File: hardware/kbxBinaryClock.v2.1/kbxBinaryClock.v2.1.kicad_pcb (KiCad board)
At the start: 2 copper layers, 127 x 114.3 mm, 137 parts, among them J1 Jack-DC, J2 Conn_01x06, J3 Conn_02x03_Odd_Even, P1 STM32_SWD_USART, Q1 2N7002, Q10 Q_NPN_BCE, Q11 Q_NPN_BCE, Q2 2N7002, Q3 2N7002, Q4 2N7002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

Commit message: Updated Silkscreen for volume mode and added clearer pin 1 markings for ICs
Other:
- board text added: "."
- board text added: "RESET SUPERVISOR"
- board text added: "RGB Binary Clock version 2.1.3 Designed by Keith Burzinski (@kbx81) in Chicago, Illinois Source & other details: https://github.com/kbx81/RGBBinaryClock Layout inspired by EKI, Inc. kit 798"
- board text removed: "RGB Binary Clock version 2.1.2 Designed by Keith Burzinski (@kbx81) in Chicago, Illinois Source & other details: https://github.com/kbx81/RGBBinaryClock Layout inspired by EKI, Inc. kit 798"
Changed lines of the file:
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@@
     (area 92.151429 32.944999 222.808572 147.514525)
     (thickness 1.6)
-    (drawings 33)
+    (drawings 41)
     (tracks 2921)
     (zones 0)
@@
       (net 158 "Net-(SB2-Pad2)"))
   )
+  (gr_text "RESET\nSUPERVISOR" (at 175.641 121.158) (layer B.SilkS)
+    (effects (font (size 0.75 0.75) (thickness 0.15)) (justify mirror))
+  )
+  (gr_text . (at 144.145 114.3) (layer F.SilkS)
+    (effects (font (size 2 2) (thickness 0.5)))
+  )
+  (gr_text . (at 160.528 117.475) (layer F.SilkS)
+    (effects (font (size 2 2) (thickness 0.5)))
+  )
+  (gr_text . (at 172.72 114.935) (layer F.SilkS)
+    (effects (font (size 2 2) (thickness 0.5)))
+  )
+  (gr_text . (at 200.787 89.789) (layer F.SilkS)
+    (effects (font (size 2 2) (thickness 0.5)))
+  )
+  (gr_text . (at 177.546 103.632) (layer F.SilkS)
+    (effects (font (size 2 2) (thickness 0.5)))
+  )
+  (gr_text . (at 147.066 103.632) (layer F.SilkS)
+    (effects (font (size 2 2) (thickness 0.5)))
+  )
+  (gr_text . (at 116.586 103.632) (layer F.SilkS)
+    (effects (font (size 2 2) (thickness 0.5)))
+  )
   (gr_text "9 to 12 Volts DC\n2 Amps\nPositive (+) Tip" (at 217.17 135.382) (layer B.SilkS)
     (effects (font (size 0.75 0.75) (thickness 0.15)) (justify left mirror))
@@
     (effects (font (size 1 1) (thickness 0.15)) (justify mirror))
   )
-  (gr_text "Touch Key Usage\n===========\n+ In Any Mode:\n A: Apply/Save\n E: Exit to Menu\n+ In \"Set Time\" Modes:\n C: Select Hour/Minute/Second\n D/U: Decrease/Increase Selected Value\n+ In \"Set Value\" Modes:\n B: Set Minimum for Value\n C: Set Maximum for Value\n D/U: Decrease/Increase Value\n+ In \"Set Color\" Modes:\n B: Select Value to Increase/Decrease by\n C: Select Color Element\n D/U: Decrease/Increase Selected Color Element\n+ In \"Set Bits\" Modes:\n B: Clear Selected Bit\n C: Set Selected Bit\n D/U: Select Previous/Next Bit" (at 187.325 131.572) (layer B.SilkS)
+  (gr_text "Touch Key Usage\n===========\n+ In Any Mode:\n A: Apply/Save\n E: Exit to Menu\n+ In \"Set Time\" Modes:\n C: Select Hour/Minute/Second\n D/U: Decrease/Increase Selected Value\n+ In \"Set Value\" Modes:\n B: Set Minimum for Value\n C: Set Maximum for Value\n D/U: Decrease/Increase Value\n+ In \"Set Color\" Modes:\n B: Select Value to Increase/Decrease by\n C: Select Color Element\n D/U: Decrease/Increase Selected Color Element\n+ In \"Set Bits\" Modes:\n B: Clear Selected Bit\n C: Set Selected Bit\n D/U: Select Previous/Next Bit" (at 170.307 130.556) (layer B.SilkS)
     (effects (font (size 0.75 0.75) (thickness 0.15)) (justify left mirror))
   )
-  (gr_text "Modes:\n====\n1: Fixed Display\n2: Toggle Display\n3: Timer/Counter\n5: Set Time\n6: Set Date\n10: Set System Options/Config Bits\n11: Set Slot Beep Enable Bits\n12: Set Slot Blink Enable Bits\n13: Set Slot Color Change Enable Bits\n20: Set Duration of Time Display Value (in Toggle Mode 2)\n21: Set Duration of Date Display Value (in Toggle Mode 2)\n22: Set Duration of Temperature Display Value (in Toggle Mode 2)\n23: Set Duration of Fade as Bits Change Value\n24: Set DST Begin Month Value\n25: Set DST Begin Day of Week Ordinal Value\n26: Set DST End Month Value\n27: Set DST End Day of Week Ordinal Value\n28: Set DST Switch Day of Week Value\n29: Set DST Switch Hour Value\n30: Set Minimum Display Intensity Value\n31: Set Flicker Reduction Threshold Value\n32: Set Current Drive Level Value\n33: Set Temperature Calibration Value\n34: Set DMX-512 Address Value\n40 - 47: Set Slot 1 through 8 Time\n50 - 57: Set Slot 1 through 8 Colors\n58: Set Date Colors\n59: Set Temperature Colors\n60: Set Timer/Counter Colors" (at 207.518 101.981) (layer B.SilkS)
+  (gr_text "Modes:\n====\n1: Fixed Display\n2: Toggle Display\n3: Timer/Counter\n5: Set Time\n6: Set Date\n10: Set System Options/Config Bits\n11: Set Slot Beep Enable Bits\n12: Set Slot Blink Enable Bits\n13: Set Slot Color Change Enable Bits\n20: Set Duration of Time Display Value (in Toggle Mode 2)\n21: Set Duration of Date Display Value (in Toggle Mode 2)\n22: Set Duration of Temperature Display Value (in Toggle Mode 2)\n23: Set Duration of Fade as Bits Change Value\n24: Set DST Begin Month Value\n25: Set DST Begin Day of Week Ordinal Value\n26: Set DST End Month Value\n27: Set DST End Day of Week Ordinal Value\n28: Set DST Switch Day of Week Value\n29: Set DST Switch Hour Value\n30: Set Minimum Display Intensity Value\n31: Set Flicker Reduction Threshold Value\n32: Set Current Drive Level Value\n33: Set Temperature Calibration Value\n34: Set Beeper (Alarm) Volume\n39: Set DMX-512 Address Value\n40 - 47: Set Slot 1 through 8 Time\n50 - 57: Set Slot 1 through 8 Colors\n58: Set Date Colors\n59: Set Temperature Colors\n60: Set Timer/Counter Colors" (at 207.518 101.981) (layer B.SilkS)
     (effects (font (size 0.75 0.75) (thickness 0.15)) (justify left mirror))
   )
@@
     (effects (font (size 1 1) (thickness 0.2)))
   )
-  (gr_text "RGB Binary Clock version 2.1.2\nDesigned by Keith Burzinski (@kbx81) in Chicago, Illinois\nSource & other details: https://github.com/kbx81/RGBBinaryClock\nLayout inspired by EKI, Inc. kit 798" (at 105.41 39.37) (layer F.SilkS)
+  (gr_text "RGB Binary Clock version 2.1.3\nDesigned by Keith Burzinski (@kbx81) in Chicago, Illinois\nSource & other details: https://github.com/kbx81/RGBBinaryClock\nLayout inspired by EKI, Inc. kit 798" (at 105.41 39.37) (layer F.SilkS)
     (effects (font (size 0.75 0.75) (thickness 0.15)) (justify left))
   )

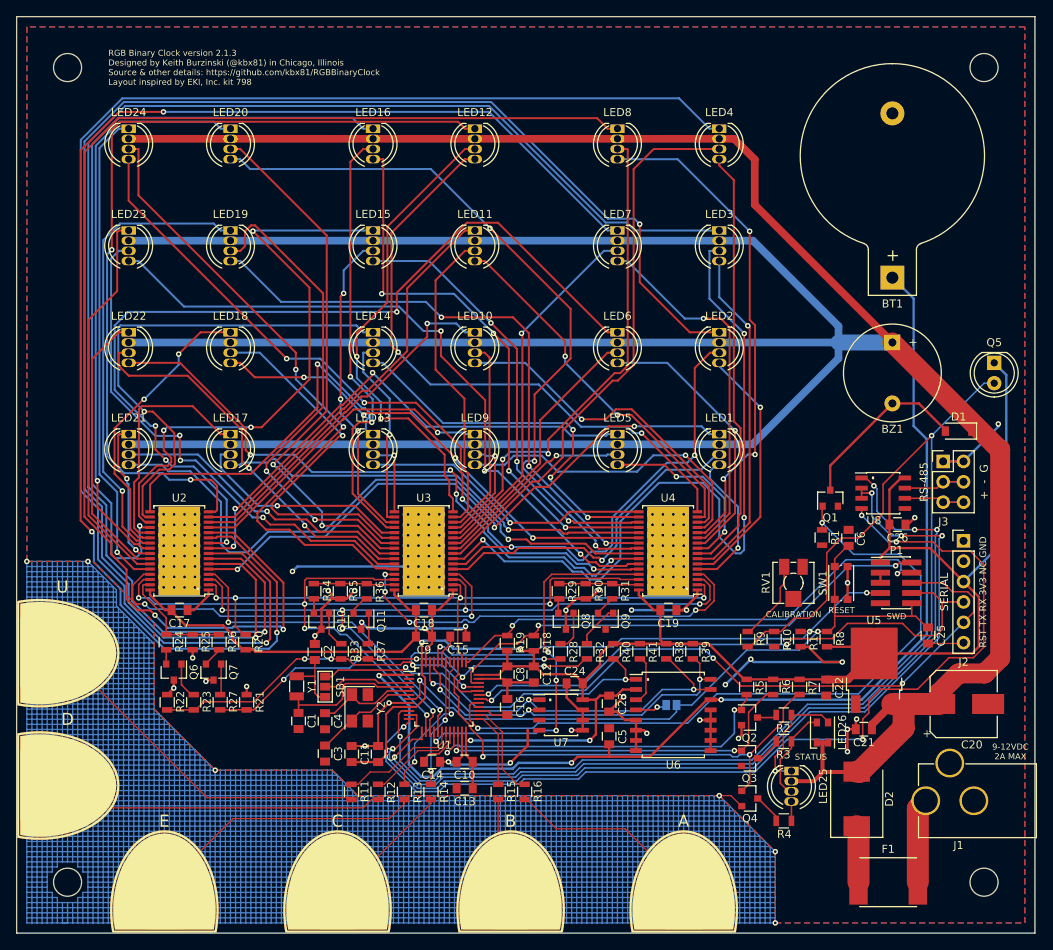
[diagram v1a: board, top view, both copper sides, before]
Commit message: Added MSOP footprint for temp sensor
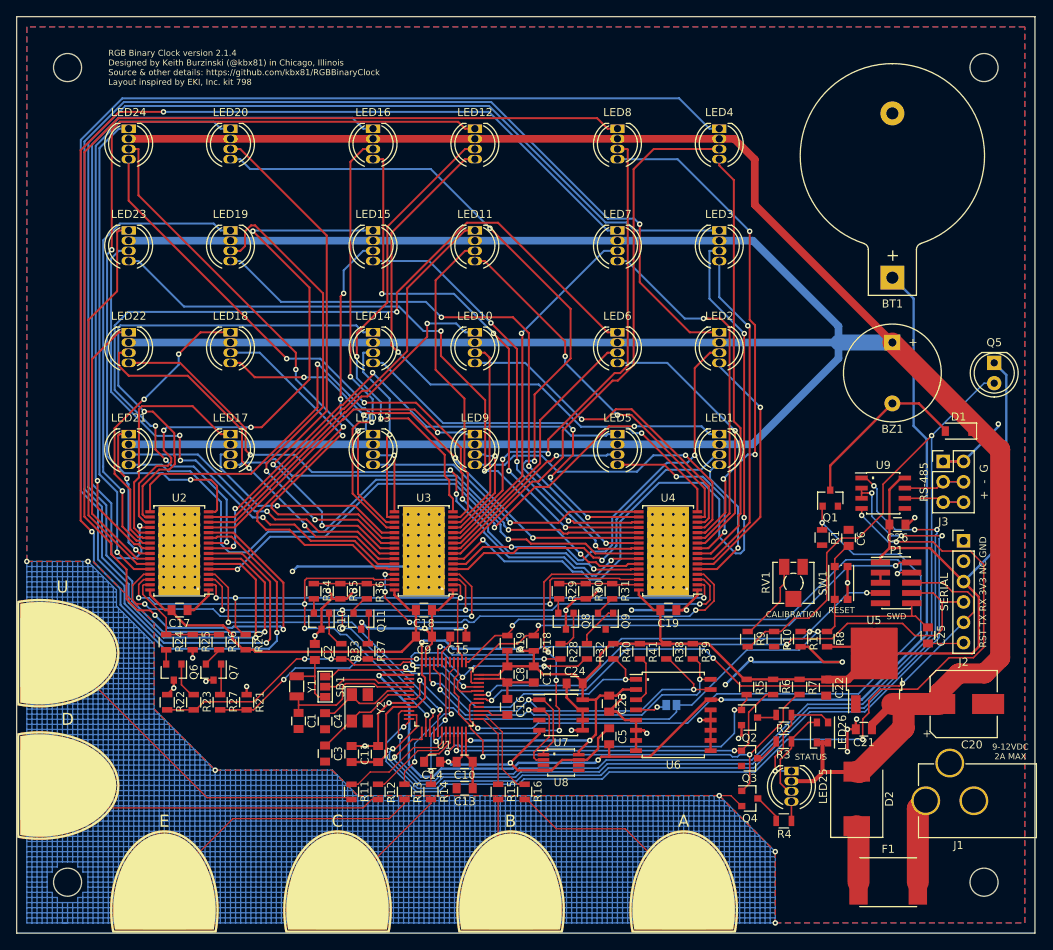
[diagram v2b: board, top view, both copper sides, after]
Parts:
- added U9: MAX485E, Housings_SOIC:SOIC-8_3.9x4.9mm_Pitch1.27mm, F.Cu at (202.1, 92.5)
- U8: value MAX485E -> MCP9804_MSOP; footprint Housings_SOIC:SOIC-8_3.9x4.9mm_Pitch1.27mm -> Housings_SSOP:MSOP-8_3x3mm_Pitch0.65mm
- moved U8 52.4 mm to (161.9, 126.0)
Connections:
- U8 pad 1: /MCU/USART2_RX -> /MCU/I2C1_SDA
- U8 pad 2: /MCU/USART2_MODE -> /MCU/I2C1_SCL
- U8 pad 3: /MCU/USART2_MODE -> Net-(U8-Pad3)
- U8 pad 4: /MCU/USART2_TX -> GND
- U8 pad 6: Net-(J3-Pad5) -> GND
- U8 pad 7: Net-(J3-Pad3) -> GND
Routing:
- net GND: track 6537.7 -> 6553.9 mm
- net /MCU/I2C1_SCL: track 46.5 -> 55.4 mm
- net /MCU/I2C1_SDA: track 47.9 -> 56.2 mm
- net +3V3: track 277.2 -> 279.5 mm
- net /Display/SPI1_MISO: track 48.2 -> 48.8 mm
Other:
- board text added: "RGB Binary Clock version 2.1.4 Designed by Keith Burzinski (@kbx81) in Chicago, Illinois Source & other details: https://github.com/kbx81/RGBBinaryClock Layout inspired by EKI, Inc. kit 798"
- board text removed: "RGB Binary Clock version 2.1.3 Designed by Keith Burzinski (@kbx81) in Chicago, Illinois Source & other details: https://github.com/kbx81/RGBBinaryClock Layout inspired by EKI, Inc. kit 798"

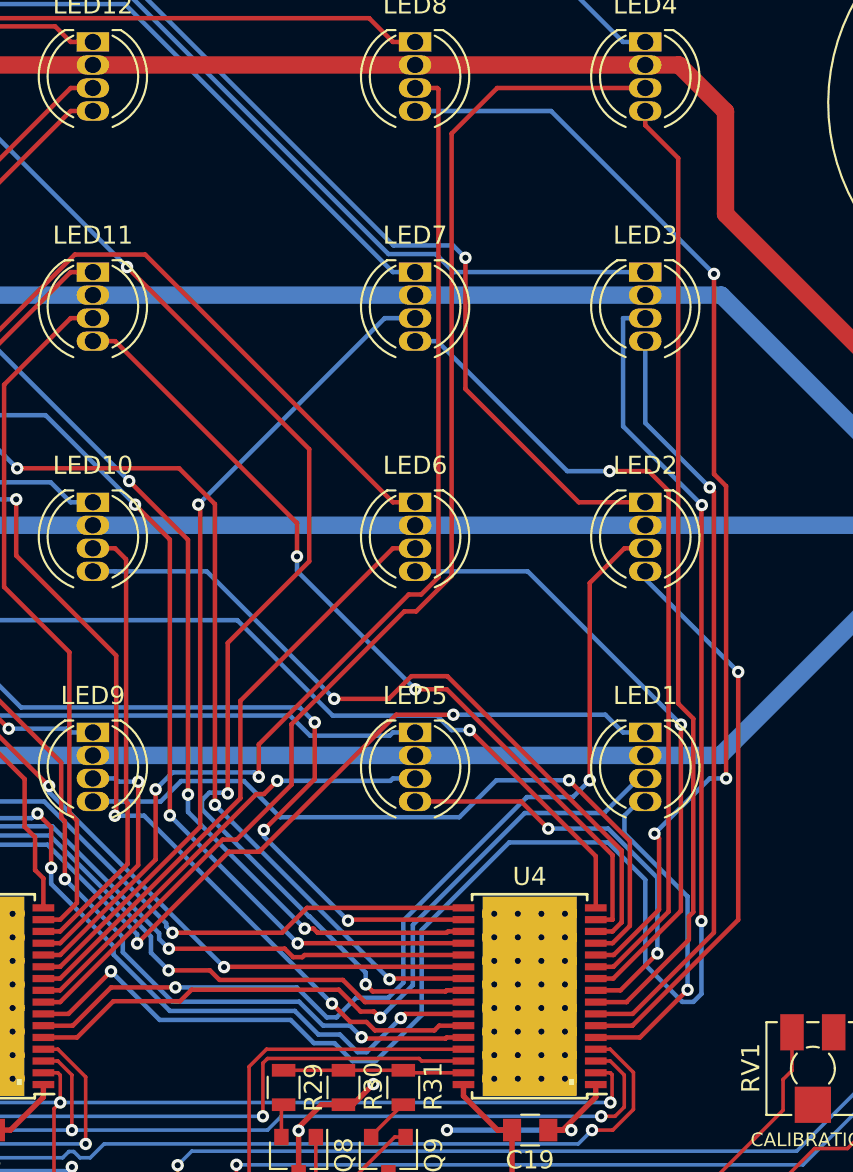
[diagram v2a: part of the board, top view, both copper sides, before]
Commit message: Updated slikscreen, minor tweaks
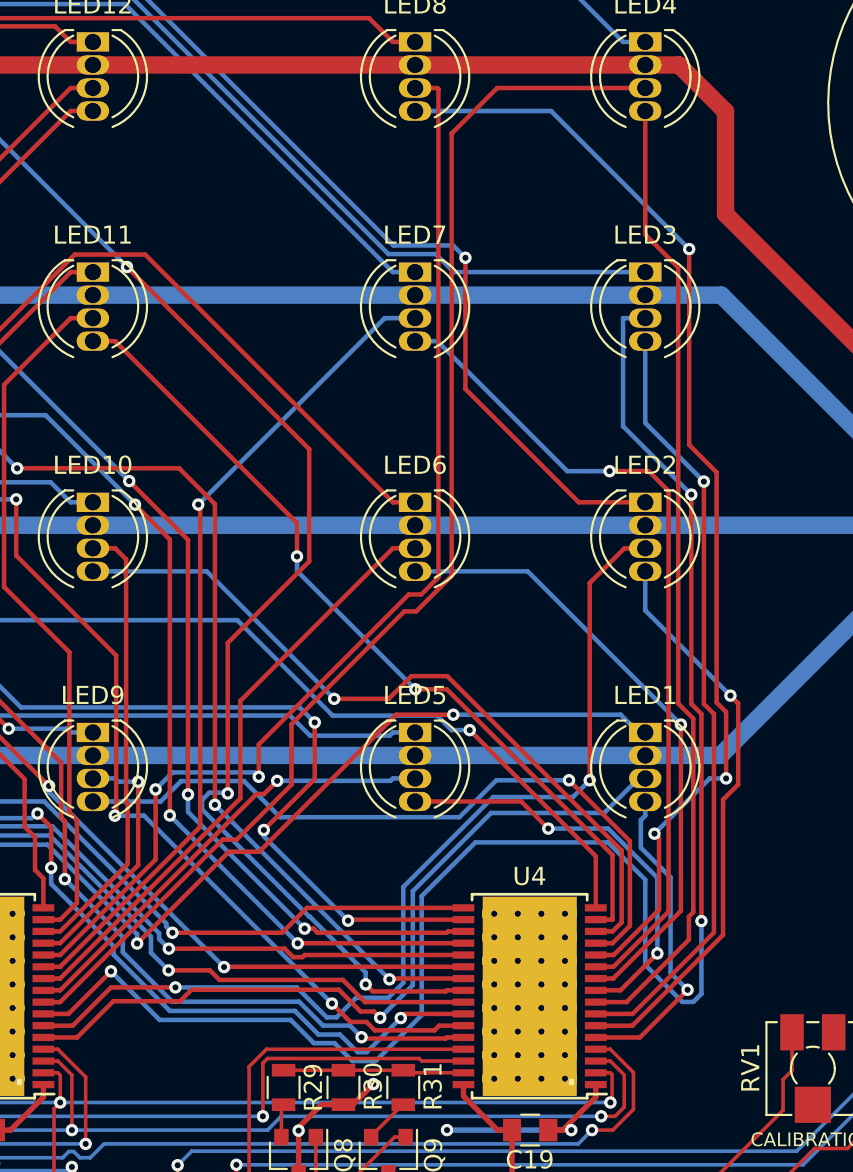
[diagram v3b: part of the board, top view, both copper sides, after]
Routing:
- net LED2_G: track 53.9 -> 55.0 mm
- net LED1_G: track 42.4 -> 43.4 mm
- net LED3_G: track 94.0 -> 95.1 mm
- net LED1_B: track 18.7 -> 17.7 mm

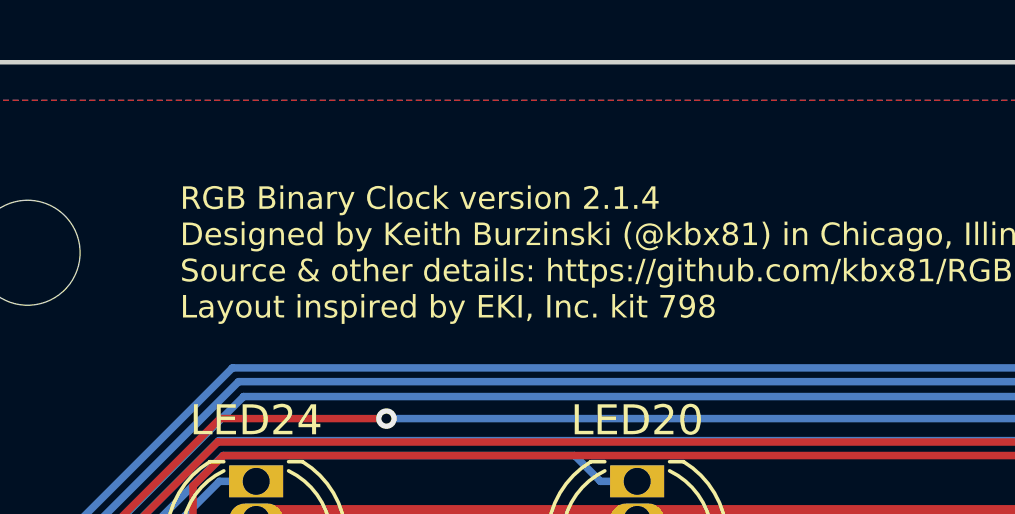
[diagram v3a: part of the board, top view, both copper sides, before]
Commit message: Updated for KiCad v5, updated silks
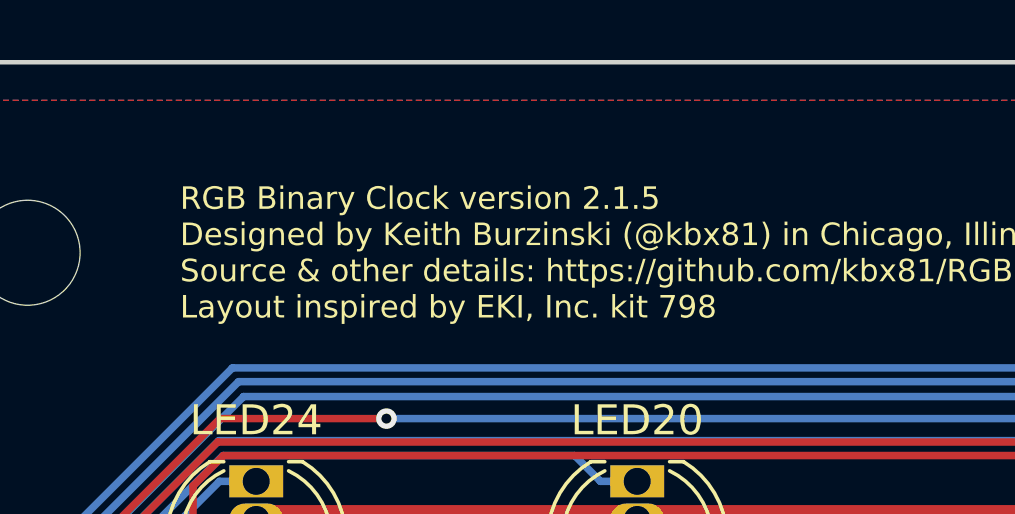
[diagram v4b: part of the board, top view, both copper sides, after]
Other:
- board text added: "DEFAULT TO TOGGLE"
- board text added: "MSbs OFF"
- board text added: "Modes: ==== 1: Fixed Display 2: Toggle Display 3: Timer/Counter 4: DMX-512 Display 5: Set Time 6: Set Date 7: Set Timer Reset Value 10: Set System Options/Config Bits 11: Set Slot Beep Enable Bits 12: Set Slot Blink Enable Bits 13: Set Slot Color Change Enable Bits 20: Set Duration of Time Display Value (in Toggle Mode 2) 21: Set Duration of Date Display Value (in Toggle Mode 2) 22: Set Duration 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"
- board text added: "RGB Binary Clock version 2.1.5 Designed by Keith Burzinski (@kbx81) in Chicago, Illinois Source & other details: https://github.com/kbx81/RGBBinaryClock Layout inspired by EKI, Inc. kit 798"
- board text removed: "Modes: ==== 1: Fixed Display 2: Toggle Display 3: Timer/Counter 5: Set Time 6: Set Date 10: Set System Options/Config Bits 11: Set Slot Beep Enable Bits 12: Set Slot Blink Enable Bits 13: Set Slot Color Change Enable Bits 20: Set Duration of Time Display Value (in Toggle Mode 2) 21: Set Duration of Date Display Value (in Toggle Mode 2) 22: Set Duration of Temperature Display Value (in Toggle Mode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"
- board text removed: "RGB Binary Clock version 2.1.4 Designed by Keith Burzinski (@kbx81) in Chicago, Illinois Source & other details: https://github.com/kbx81/RGBBinaryClock Layout inspired by EKI, Inc. kit 798"
